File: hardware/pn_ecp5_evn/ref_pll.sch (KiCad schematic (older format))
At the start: 37 parts, among them J601 Conn_Coaxial, U601 LM2904, U602 OPA2211, X601 ABLNO

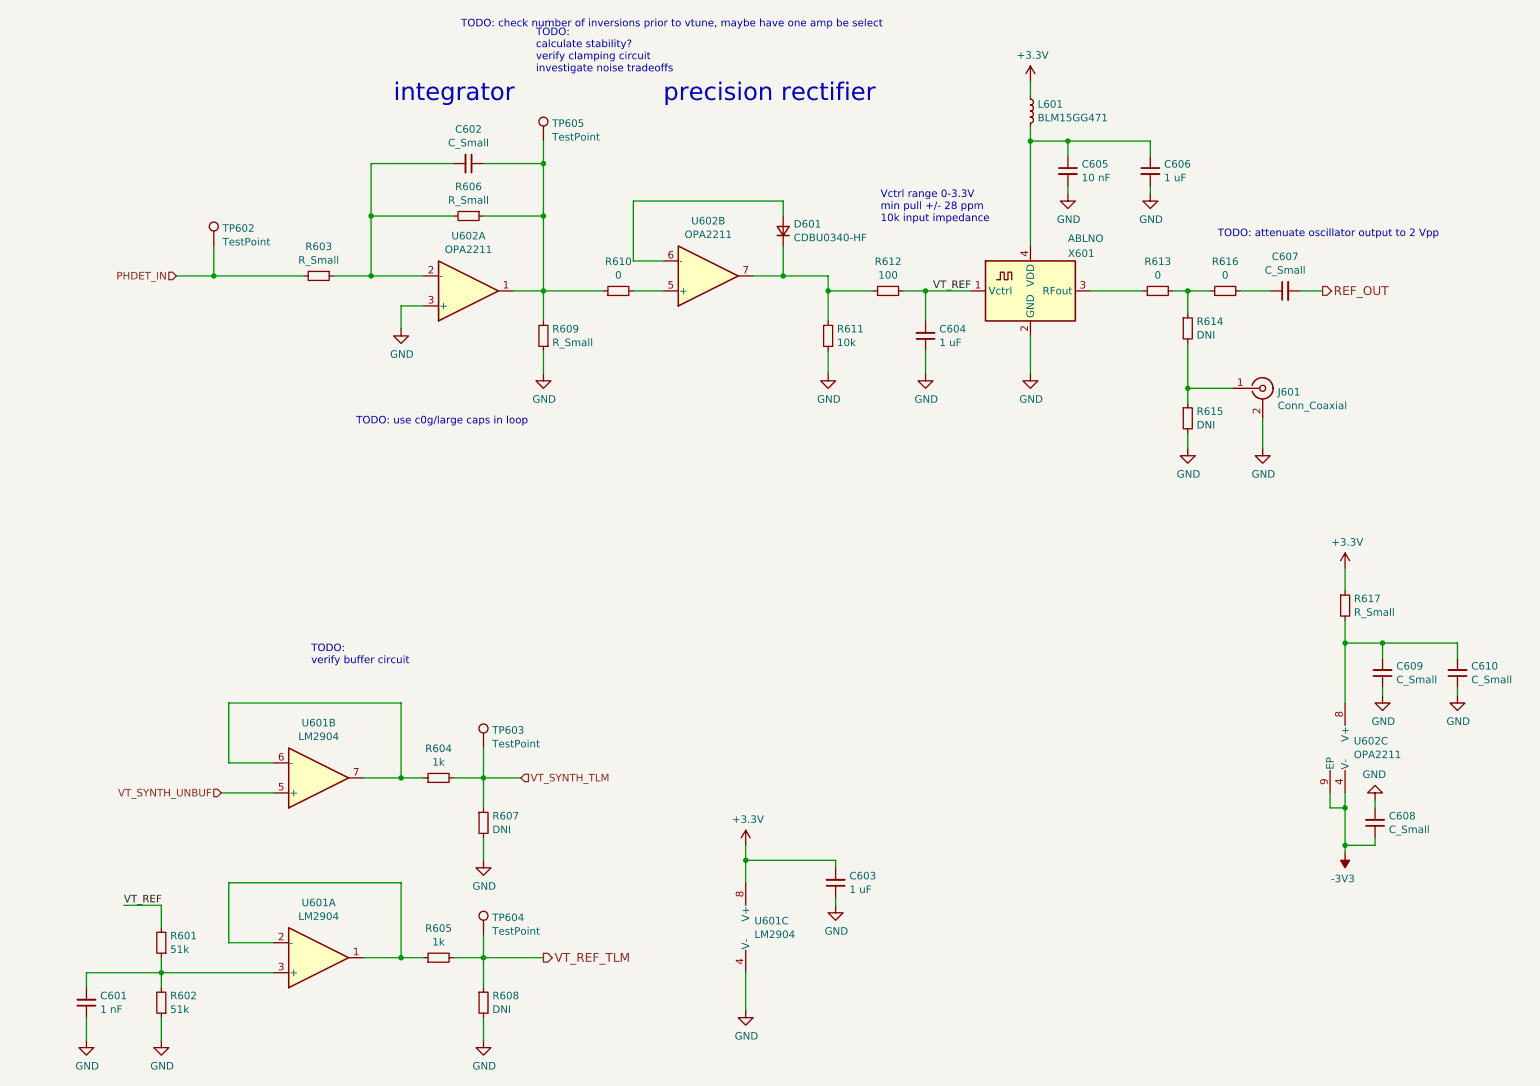
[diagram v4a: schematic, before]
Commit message: checked stability of LO amplifier, started migen project, added more flexibility for active filtering on baseband path
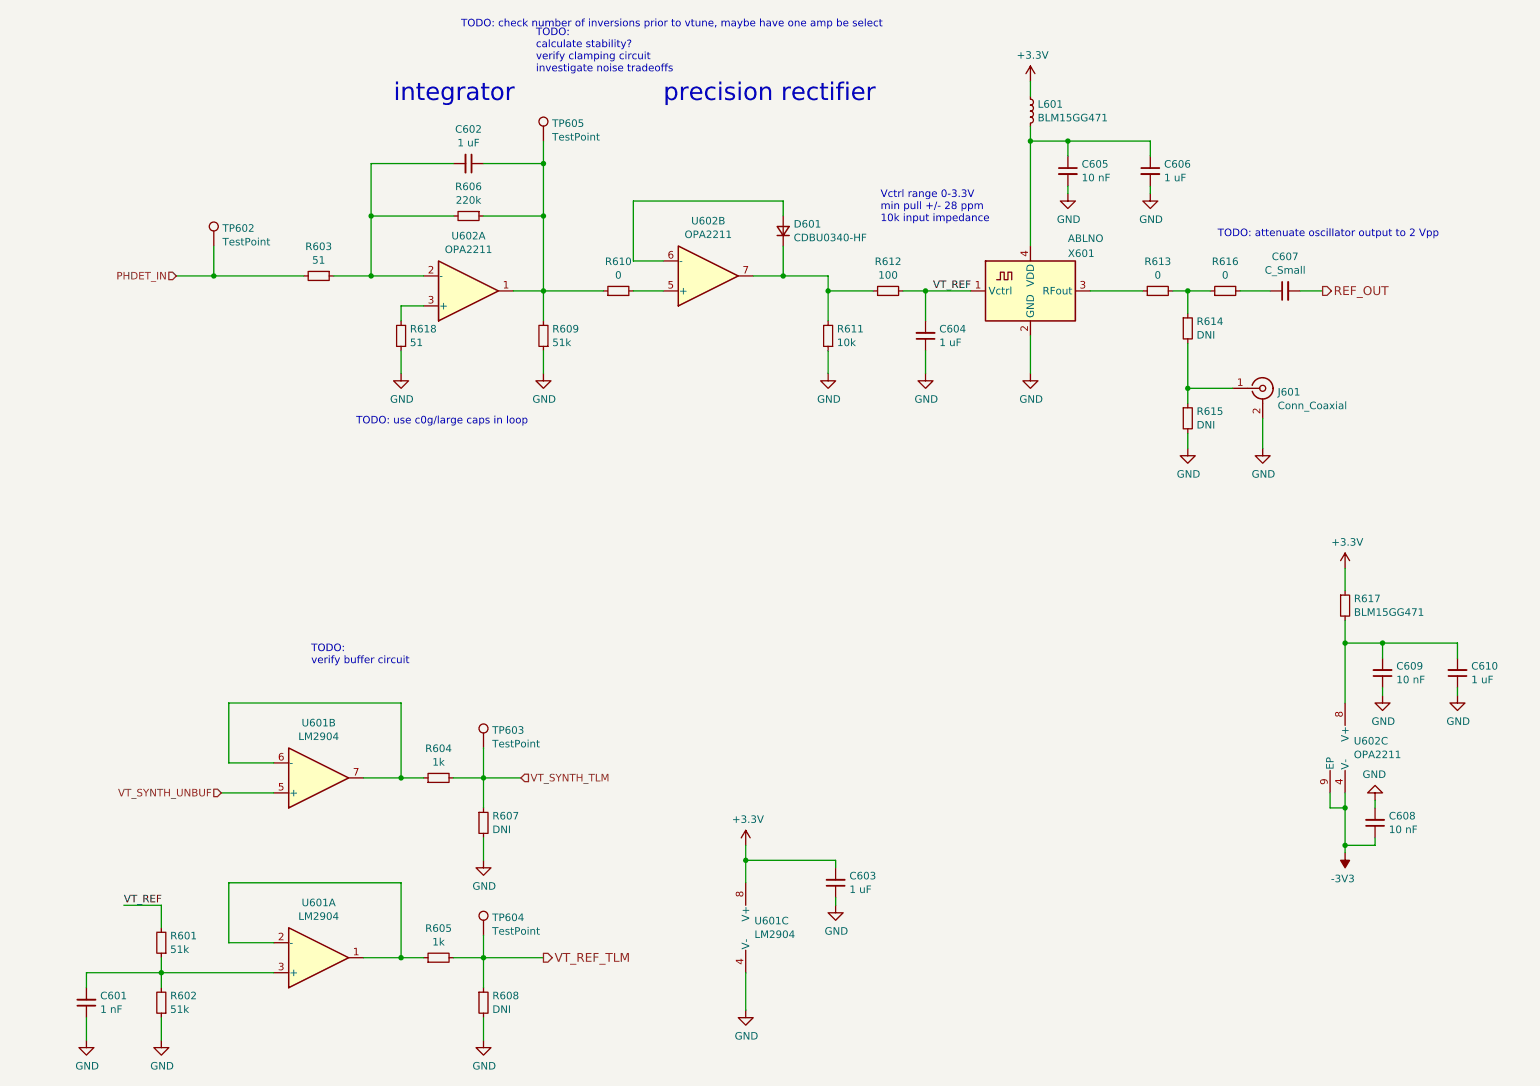
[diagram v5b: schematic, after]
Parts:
- added R618: 51, Resistor_SMD:R_0402_1005Metric, symbol Device:R_Small
- C602, C610: value C_Small -> 1 uF
- C608, C609: value C_Small -> 10 nF
- R603: value R_Small -> 51
- R606: value R_Small -> 220k
- R609: value R_Small -> 51k
- R617: value R_Small -> BLM15GG471
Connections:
- net GND: now also R618.1; no longer U602.3 (+)
- new net: R618.2, U602.3 (+)
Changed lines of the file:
@@
 L power:GND #PWR?
 U 1 1 5F4F2733
-P 3200 2650
+P 3200 2950
 AR Path="/5F265927/5F4F2733" Ref="#PWR?"  Part="1"
 AR Path="/5F4ECD93/5F4F2733" Ref="#PWR0201"  Part="1"
-F 0 "#PWR0201" H 3200 2400 50  0001 C CNN
-F 1 "GND" H 3205 2477 50  0000 C CNN
-F 2 "" H 3200 2650 50  0001 C CNN
-F 3 "" H 3200 2650 50  0001 C CNN
-	1    3200 2650
+F 0 "#PWR0201" H 3200 2700 50  0001 C CNN
+F 1 "GND" H 3205 2777 50  0000 C CNN
+F 2 "" H 3200 2950 50  0001 C CNN
+F 3 "" H 3200 2950 50  0001 C CNN
+	1    3200 2950
 	1    0    0    -1
 $EndComp
@@
 Wire Wire Line
 	3200 2500 3350 2500
-Wire Wire Line
-	3200 2500 3200 2650
 $Comp
 L Device:R_Small R?
@@
 AR Path="/5F4ECD93/5F4F273D" Ref="R603"  Part="1"
 F 0 "R603" V 2454 2300 50  0000 C CNN
-F 1 "R_Small" V 2545 2300 50  0000 C CNN
+F 1 "51" V 2545 2300 50  0000 C CNN
 F 2 "Resistor_SMD:R_0402_1005Metric" H 2650 2300 50  0001 C CNN
 F 3 "~" H 2650 2300 50  0001 C CNN
@@
 AR Path="/5F4ECD93/5F4F2749" Ref="R609"  Part="1"
 F 0 "R609" H 4091 2654 50  0000 R CNN
-F 1 "R_Small" H 4091 2745 50  0000 R CNN
+F 1 "51k" H 4091 2745 50  0000 R CNN
 F 2 "Resistor_SMD:R_0402_1005Metric" H 4150 2700 50  0001 C CNN
 F 3 "~" H 4150 2700 50  0001 C CNN
@@
 AR Path="/5F4ECD93/5F4F2753" Ref="R606"  Part="1"
 F 0 "R606" V 3454 1900 50  0000 C CNN
-F 1 "R_Small" V 3545 1900 50  0000 C CNN
+F 1 "220k" V 3545 1900 50  0000 C CNN
 F 2 "Resistor_SMD:R_0402_1005Metric" H 3650 1900 50  0001 C CNN
 F 3 "~" H 3650 1900 50  0001 C CNN
@@
 AR Path="/5F4ECD93/5F4F2759" Ref="C602"  Part="1"
 F 0 "C602" V 3421 1550 50  0000 C CNN
-F 1 "C_Small" V 3512 1550 50  0000 C CNN
+F 1 "1 uF" V 3512 1550 50  0000 C CNN
 F 2 "Capacitor_SMD:C_0603_1608Metric" H 3650 1550 50  0001 C CNN
 F 3 "~" H 3650 1550 50  0001 C CNN
@@
 AR Path="/5F4ECD93/5F4F27F8" Ref="R617"  Part="1"
 F 0 "R617" H 9559 4546 50  0000 L CNN
-F 1 "R_Small" H 9559 4455 50  0000 L CNN
+F 1 "BLM15GG471" H 9559 4455 50  0000 L CNN
 F 2 "Resistor_SMD:R_0402_1005Metric" H 9500 4500 50  0001 C CNN
 F 3 "~" H 9500 4500 50  0001 C CNN
@@
 AR Path="/5F4ECD93/5F4F280C" Ref="C610"  Part="1"
 F 0 "C610" H 10158 4904 50  0000 R CNN
-F 1 "C_Small" H 10158 4995 50  0000 R CNN
+F 1 "1 uF" H 10158 4995 50  0000 R CNN
 F 2 "Capacitor_SMD:C_0402_1005Metric" H 10250 4950 50  0001 C CNN
 F 3 "~" H 10250 4950 50  0001 C CNN
@@
 AR Path="/5F4ECD93/5F4F2812" Ref="C609"  Part="1"
 F 0 "C609" H 9658 4904 50  0000 R CNN
-F 1 "C_Small" H 9658 4995 50  0000 R CNN
+F 1 "10 nF" H 9658 4995 50  0000 R CNN
 F 2 "Capacitor_SMD:C_0402_1005Metric" H 9750 4950 50  0001 C CNN
 F 3 "~" H 9750 4950 50  0001 C CNN
@@
 AR Path="/5F4ECD93/5F4F2823" Ref="C608"  Part="1"
 F 0 "C608" H 9608 5904 50  0000 R CNN
-F 1 "C_Small" H 9608 5995 50  0000 R CNN
+F 1 "10 nF" H 9608 5995 50  0000 R CNN
 F 2 "Capacitor_SMD:C_0402_1005Metric" H 9700 5950 50  0001 C CNN
 F 3 "~" H 9700 5950 50  0001 C CNN
@@
 	1    0    0    -1
 $EndComp
+$Comp
+L Device:R_Small R?
+U 1 1 5F521DBB
+P 3200 2700
+AR Path="/5F265927/5F521DBB" Ref="R?"  Part="1"
+AR Path="/5F4ECD93/5F521DBB" Ref="R618"  Part="1"
+F 0 "R618" H 3141 2654 50  0000 R CNN
+F 1 "51" H 3141 2745 50  0000 R CNN
+F 2 "Resistor_SMD:R_0402_1005Metric" H 3200 2700 50  0001 C CNN
+F 3 "~" H 3200 2700 50  0001 C CNN
+	1    3200 2700
+	-1   0    0    1
+$EndComp
+Wire Wire Line
+	3200 2800 3200 2950
+Wire Wire Line
+	3200 2500 3200 2600
 $EndSCHEMATC

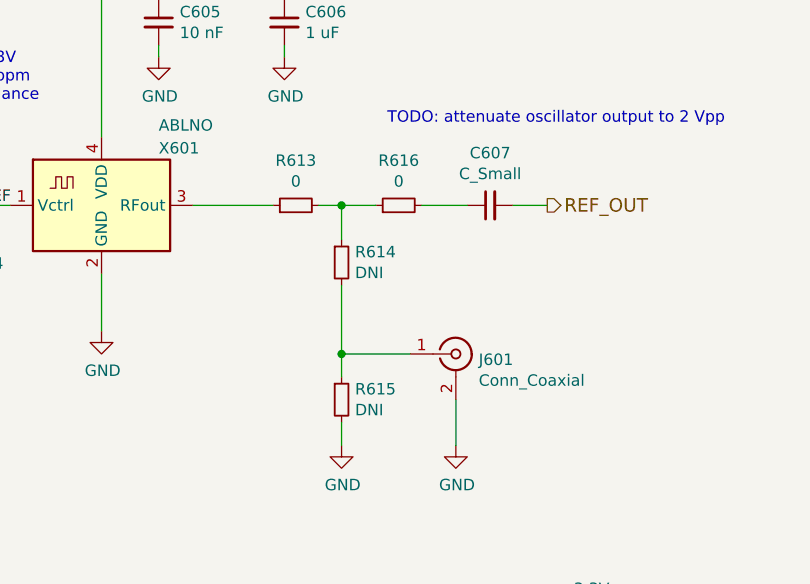
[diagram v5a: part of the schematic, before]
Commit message: added part numbers to schematic of phase noise downconverter, ordered
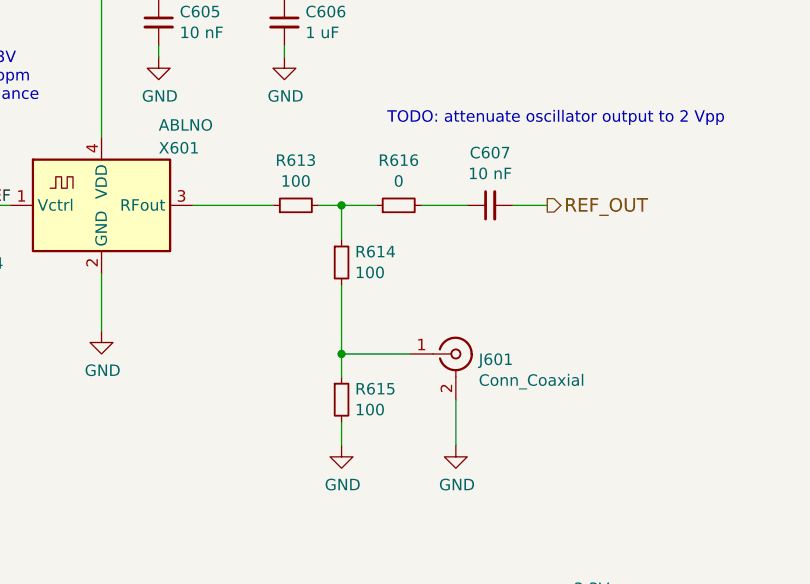
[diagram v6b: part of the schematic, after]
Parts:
- C601, C602, C603, C604, C605, C606, C608, C609, C610, J601, R601, R602, R603, R606, R607, R608, R609, R611, R618: Distributor Part Number (none) -> N/A
- C607: value C_Small -> 10 nF; Distributor Part Number (none) -> N/A
- D601: Distributor (none) -> Digi-Key; Distributor Part Number (none) -> 641-2065-1-ND
- L601, R617: Distributor (none) -> Digi-Key; Distributor Part Number (none) -> 490-5198-1-ND
- R604, R605: Distributor (none) -> Digi-Key; Distributor Part Number (none) -> RR05P1.0KDCT-ND
- R610, R616: Distributor (none) -> Digi-Key; Distributor Part Number (none) -> P0.0JCT-ND
- R612: Distributor (none) -> Digi-Key; Distributor Part Number (none) -> RR05P100DCT-ND
- R613: value 0 -> 100; Distributor (none) -> Digi-Key; Distributor Part Number (none) -> RR05P100DCT-ND
- R614, R615: value DNI -> 100; Distributor (none) -> Digi-Key; Distributor Part Number (none) -> RR05P100DCT-ND
- TP602, TP603, TP604, TP605: Distributor (none) -> Digi-Key; Distributor Part Number (none) -> 36-5015CT-ND
- U601: Distributor (none) -> Digi-Key; Distributor Part Number (none) -> 296-17931-1-ND
- U602: Distributor (none) -> Digi-Key; Distributor Part Number (none) -> 296-43607-1-ND
- X601: Distributor (none) -> Digi-Key; Distributor Part Number (none) -> 535-12341-1-ND

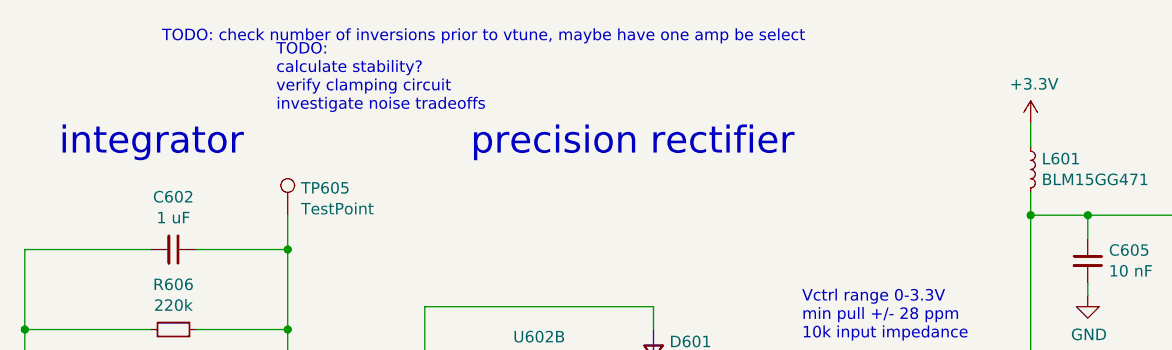
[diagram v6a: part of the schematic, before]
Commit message: added schematic export, updated README, schematic cleanup
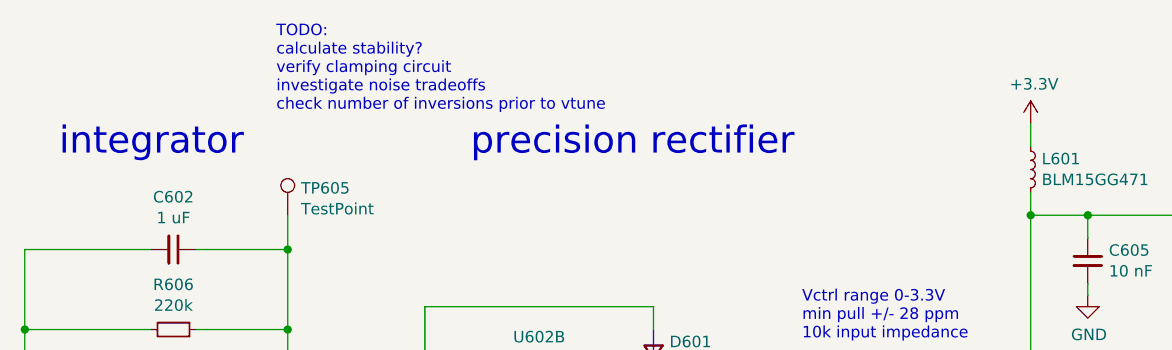
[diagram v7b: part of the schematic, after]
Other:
- note added: "TODO:\ncalculate stability?\nverify clamping circuit\ninvestigate noise tradeoffs\ncheck number of inversions prior to vtune"
- note removed: "TODO: check number of inversions prior to vtune, maybe have one amp be select"
- note removed: "TODO:\ncalculate stability?\nverify clamping circuit\ninvestigate noise tradeoffs"
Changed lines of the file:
@@
 PHDET_IN
 Text Notes 4100 950  0    50   ~ 0
-TODO:\ncalculate stability?\nverify clamping circuit\ninvestigate noise tradeoffs
+TODO:\ncalculate stability?\nverify clamping circuit\ninvestigate noise tradeoffs\ncheck number of inversions prior to vtune
 Text Notes 2600 4900 0    50   ~ 0
 TODO:\nverify buffer circuit
-Text Notes 3600 650  0    50   ~ 0
-TODO: check number of inversions prior to vtune, maybe have one amp be select
 Text Notes 3150 1150 0    118  ~ 0
 integrator

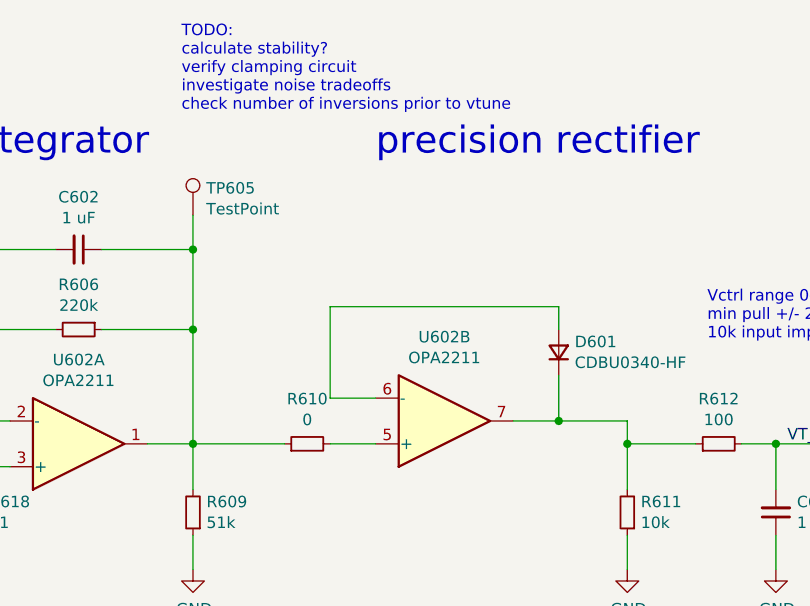
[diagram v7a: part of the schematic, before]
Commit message: fixed rectifier circuit, inverted first lna to cancel out inverting integrator..
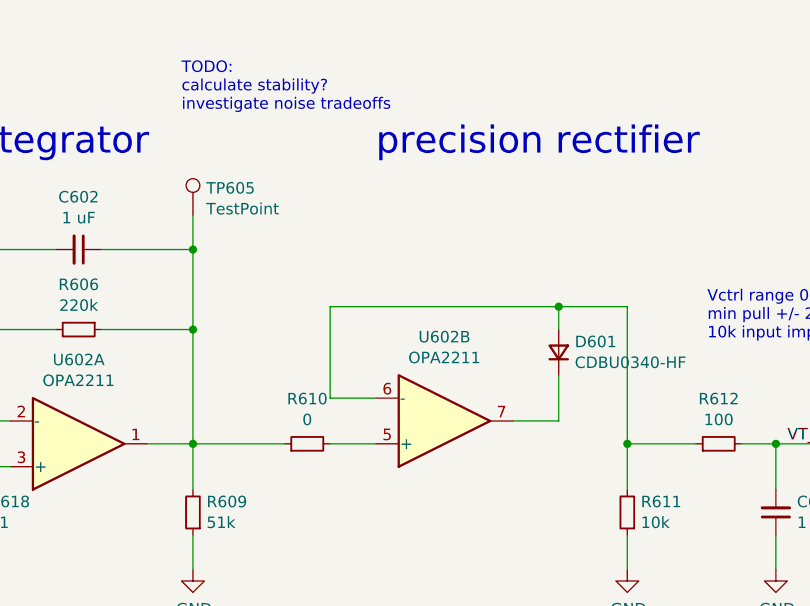
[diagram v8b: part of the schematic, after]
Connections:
- net at R611.2, R612.1: now also D601.2 (A), U602.6 (-); no longer D601.1 (K), U602.7
- new net: D601.1 (K), U602.7
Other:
- note added: "TODO:\ncalculate stability?\ninvestigate noise tradeoffs"
- note removed: "TODO:\ncalculate stability?\nverify clamping circuit\ninvestigate noise tradeoffs\ncheck number of inversions prior to vtune"
